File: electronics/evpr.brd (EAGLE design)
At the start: 97.2 x 71.7 mm, 89 parts, among them J1 10118193-0001LF, J2 B4P-VH(LF)(SN), Q1 AOD4184A, Q2 AOD4184A, T1 MMBT2222A, T2 MMBT2222A, T3 MMBT2222A, T5 MMBT2222A, U1 MC14044BDR2G, U2 BQ2057TTS, U3 ESP32-WROOM-32D, U5 AP2112K-3.3TRG1, U6 SN74AHCT125DR, U7 TPSM84824MOLR, U8 LTC4353CMSPBFMSOP-16_MS-M, X1 B3P-VH(LF)(SN), X2 B3P-VH(LF)(SN), X3 B3P-VH(LF)(SN)

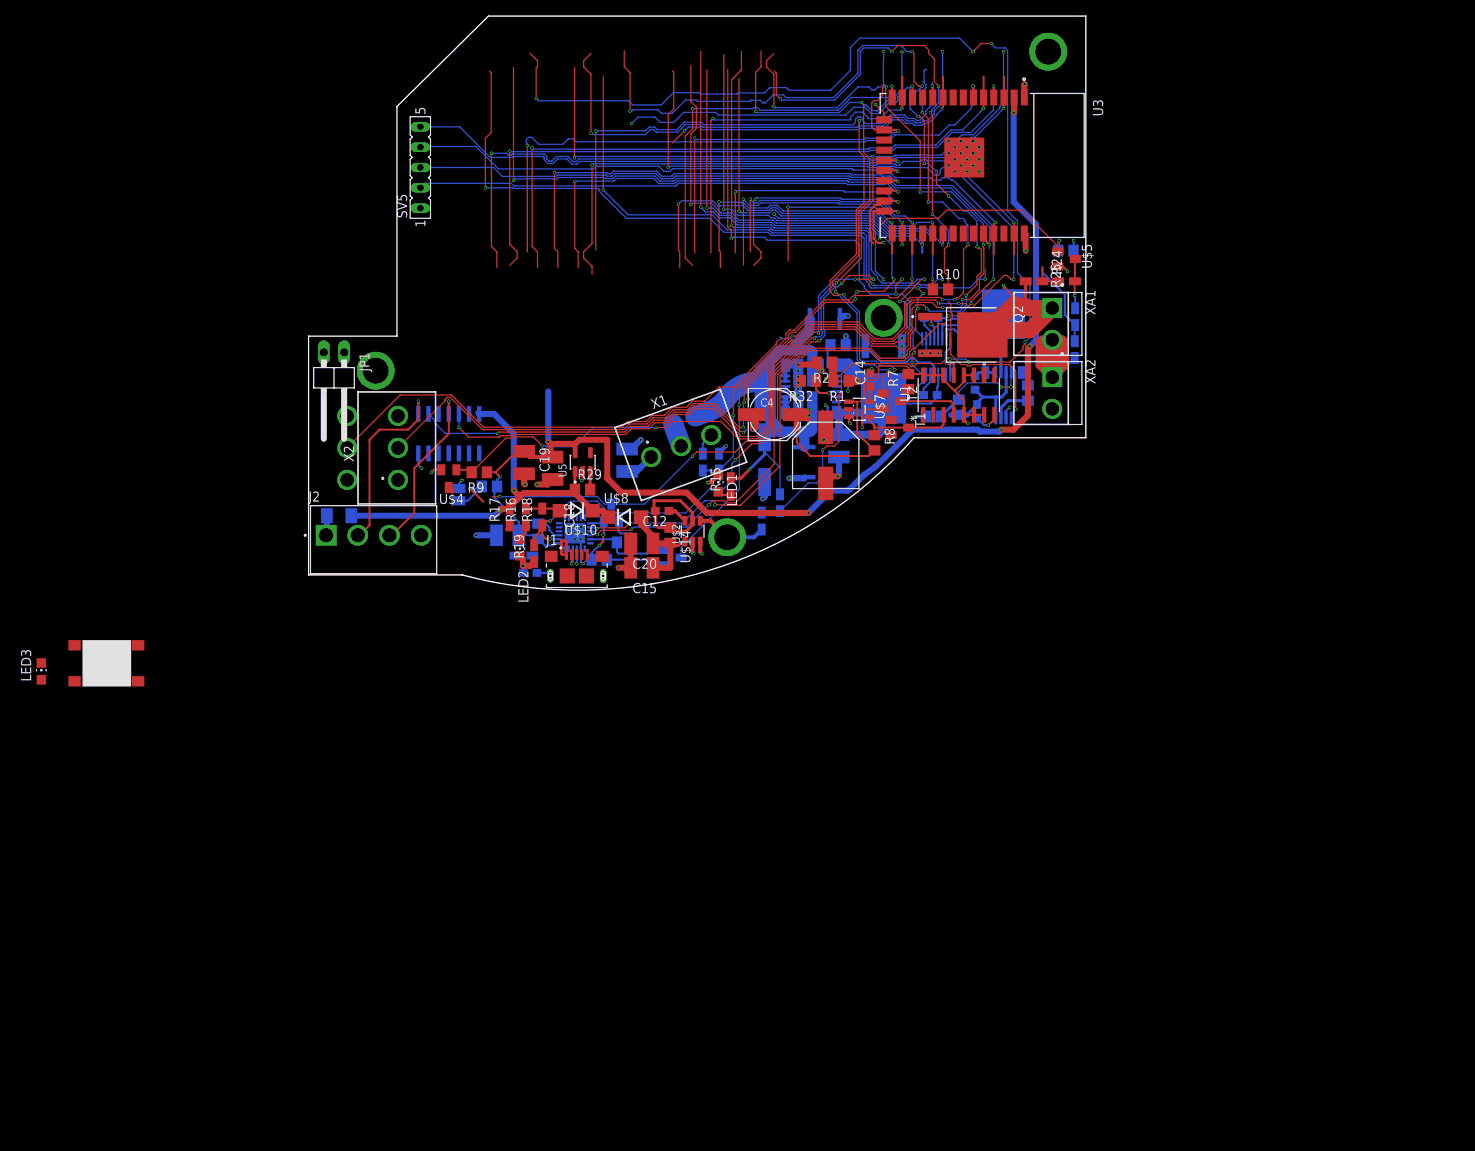
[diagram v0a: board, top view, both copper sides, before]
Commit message: Fixed power save for battery sensing
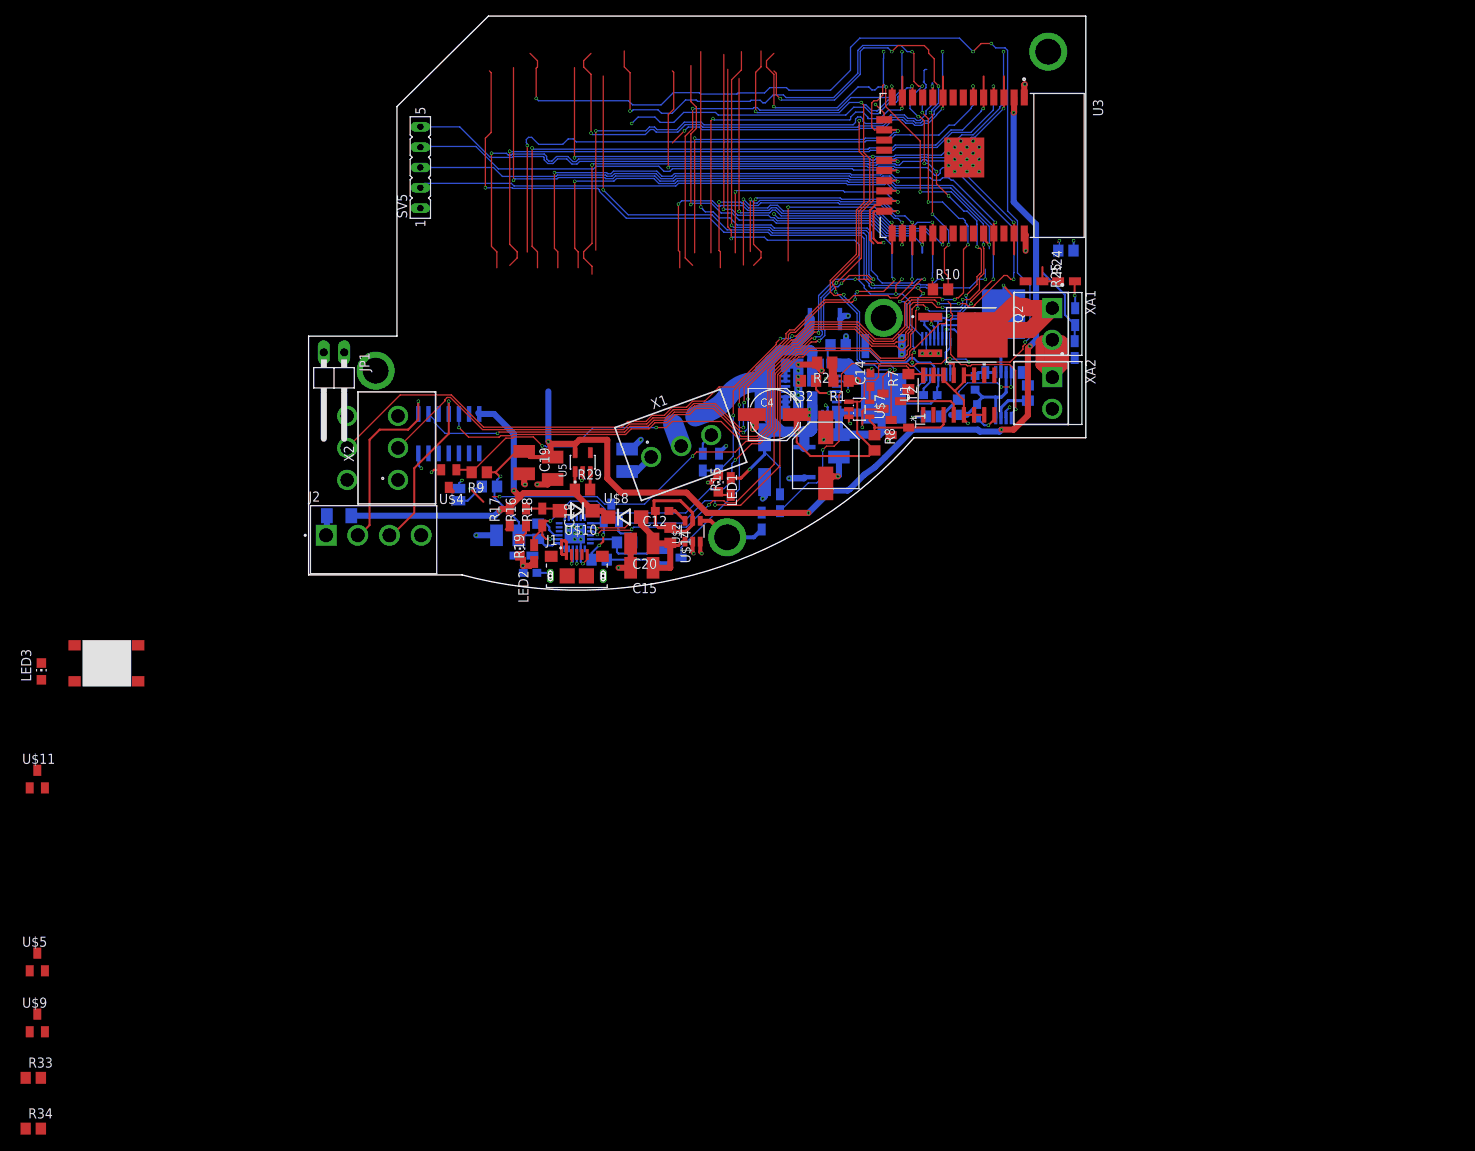
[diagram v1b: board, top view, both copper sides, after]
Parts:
- added R33, R34: 100k, rcl:R0805
- added U$11: DMN5L06K-7, mccloud:SOT23
- added U$9: BSS84-7-F, mccloud:SOT23
- U$5: value DMN5L06K-7 -> BSS84-7-F
- moved U$5 155.8 mm to (-67.6, -102.4), turned to 0 degrees
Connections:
- new net N$13: R24.2, U$9.3
- new net N$35: R33.2, U$11.3, U$5.1, U$9.1
- net GND: now also R25.1, R27.1, R34.2, U$11.2; no longer U$5.2
- net N$33: now also R26.2; no longer R25.1, R27.1
- net N$8: now also U$5.2; no longer R26.2
- net POWERSAVE: now also R34.1, U$11.1; no longer U$5.1
- net VBAT: now also R33.1, U$9.2; no longer R24.2
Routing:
- net POWERSAVE: track 112.5 -> 37.3 mm, vias 7 -> 4
- net N$33: track 6.22 -> 0.00 mm, vias 1 -> 0
- net N$8: track 21.8 -> 18.4 mm
- net VBAT: track 56.1 -> 53.5 mm
- net GND: track 109.5 -> 111.4 mm

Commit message: routing and board fixes
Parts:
- added U$13, U$15: LSM115J, mccloud:DO214BA
- C1: value 10sµF -> 10µF
- moved R34 98.1 mm to (1.27, -53.8), turned to 180 degrees
- moved XA1 92.9 mm to (-29.5, -50.0), turned to 180 degrees
- moved XA2 89.8 mm to (-29.5, -44.7), flipped to the bottom, turned to 180 degrees
- moved R33 85.8 mm to (-14.0, -50.3), flipped to the bottom, turned to 180 degrees
- moved U$9 80.3 mm to (-11.4, -52.6), flipped to the bottom, turned to 270 degrees
- moved U$5 77.8 mm to (-10.4, -49.5), flipped to the bottom, turned to 90 degrees
- moved U$3 77.7 mm to (-19.8, -50.3), flipped to the top, turned to 90 degrees
- moved X3 76.4 mm to (45.2, -57.0), turned to 0 degrees
- moved U$11 74.2 mm to (1.14, -51.4), turned to 90 degrees
- moved Q2 73.0 mm to (-19.8, -50.5), flipped to the bottom
- moved R26 72.5 mm to (-6.35, -49.5), turned to 0 degrees
- moved R4 71.8 mm to (-12.2, -52.8), flipped to the top, turned to 180 degrees
- moved R14 70.9 mm to (55.8, -5.08)
- moved T3 70.8 mm to (57.5, 0.25)
- moved U$12 69.6 mm to (51.1, -1.91), turned to 180 degrees
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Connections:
- new net AGND: R2.2, R31.2, R32.2, U7.23, U7.3, U7.9
- new net N$43: R7.2, R8.2, U$13.C, U$15.C, U1.11, U1.12, U1.14, U1.15, U1.16, U1.5, U1.6, U1.7
- net GND: no longer R2.2, R31.2, R32.2, U7.23, U7.3, U7.9
- net VBAT: now also U$15.A
- net VRAW: now also U$13.A; no longer R7.2, R8.2, U1.11, U1.12, U1.14, U1.15, U1.16, U1.5, U1.6, U1.7
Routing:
- net RESET: track 248.2 -> 0.00 mm, vias 10 -> 0
- net SERVO1: track 240.6 -> 0.00 mm, vias 8 -> 0
- net RAWSENSE: track 236.7 -> 0.00 mm, vias 9 -> 0
- net ESP_TX: track 231.3 -> 0.00 mm, vias 9 -> 0
- net ESP_RX: track 224.1 -> 0.00 mm, vias 10 -> 0
- net DS_DAT: track 212.7 -> 0.00 mm, vias 13 -> 0
- net DS_CLK: track 198.5 -> 0.00 mm, vias 12 -> 0
- net SERVO2: track 189.6 -> 0.00 mm, vias 9 -> 0
- net RST_DISABLE: track 182.6 -> 0.00 mm, vias 9 -> 0
- net USBSENSE: track 152.7 -> 0.00 mm, vias 9 -> 0
- net SHUTDOWN_CANCEL: track 150.9 -> 0.00 mm, vias 7 -> 0
- net 3.3V: track 149.9 -> 0.00 mm, vias 6 -> 0
- net CSTAT: track 130.8 -> 0.00 mm, vias 9 -> 0
- net BOOTMODE: track 124.0 -> 0.00 mm, vias 7 -> 0
- net SHUTDOWN: track 123.1 -> 0.00 mm, vias 7 -> 0
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
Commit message: Whew. Lots of routing. Lots of minor circuit changes. Routing is 99% done, just finishing touches are remaining.
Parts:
- removed R11: 10k, rcl:R0805
- added C11, C21: 0.1uF, eagle-ltspice:C0603
- U$13: value LSM115J -> SDM40E20LC; device mccloud:DO214BA -> mccloud:SOT23
- U$15: value LSM115J -> 1000µF; device mccloud:DO214BA -> mccloud:810RADCAN
- moved C13 111.7 mm to (-8.89, -48.4), flipped to the top, turned to 0 degrees
- moved R25 111.7 mm to (-2.41, -52.6), flipped to the bottom, turned to 0 degrees
- moved R24 107.8 mm to (-6.35, -54.4), flipped to the bottom, turned to 0 degrees
- moved R15 106.9 mm to (-27.4, -41.6), turned to 0 degrees
- moved LED3 105.9 mm to (34.5, -36.3), flipped to the bottom
- moved R1 102.1 mm to (-12.7, -37.3), turned to 90 degrees
- moved U$1 102.0 mm to (35.1, -25.4)
- moved R32 101.6 mm to (-16.3, -37.3), turned to 90 degrees
- moved R2 100.9 mm to (-14.5, -37.3), turned to 270 degrees
- moved C5 96.8 mm to (-2.92, -37.7), turned to 180 degrees
- moved C10 96.8 mm to (-4.83, -39.4), turned to 180 degrees
- moved C9 94.8 mm to (43.9, -19.3), flipped to the top
- moved J1 92.6 mm to (38.4, -19.3), flipped to the bottom, turned to 180 degrees
- moved LED1 91.5 mm to (-31.1, -41.6), turned to 90 degrees
- moved J2 90.1 mm to (49.7, -32.3)
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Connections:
- net 5.0V: now also C21.2
- net GND: now also C11.1, C21.1, U$15.C$2; no longer R11.1
- net N$28: now also U$15.A$1
- net N$43: now also C11.2, U$13.3; no longer U$13.C, U$15.C
- net POWERSAVE: no longer R11.2
- net VBAT: now also U$13.1; no longer U$15.A
- net VRAW: now also U$13.2; no longer U$13.A
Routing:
- net CSTAT: track 0.00 -> 51.0 mm, vias 0 -> 2
- net 3.3V: track 0.00 -> 49.2 mm, vias 0 -> 4
- net VRAW: track 71.8 -> 120.9 mm, vias 8 -> 14
- net POWERSAVE: track 0.00 -> 49.0 mm, vias 0 -> 1
- net USING_BAT: track 0.00 -> 48.7 mm, vias 0 -> 2
- net 5.0V: track 0.00 -> 46.6 mm, vias 0 -> 3
- net VCONV: track 40.2 -> 85.0 mm, vias 8 -> 10
- net USING_ENG: track 0.00 -> 42.2 mm, vias 0 -> 2
- net TACH: track 38.6 -> 78.2 mm, vias 0 -> 2
- net RESET: track 0.00 -> 39.5 mm, vias 0 -> 3
- net N$43: track 0.00 -> 34.9 mm, vias 0 -> 1
- net VBAT: track 28.1 -> 59.6 mm, vias 0 -> 5
- net RAWSENSE: track 0.00 -> 26.5 mm, vias 0 -> 2
- net BATSENSE1: track 0.00 -> 26.4 mm, vias 0 -> 2
- net BATSENSE2: track 0.00 -> 23.5 mm, vias 0 -> 2
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- added copper zone on layer 1, net AGND
- added copper zone on layer 15, net AGND
- added copper zone on layer 16, net AGND
- added copper zone on layer 1, net AVOID1

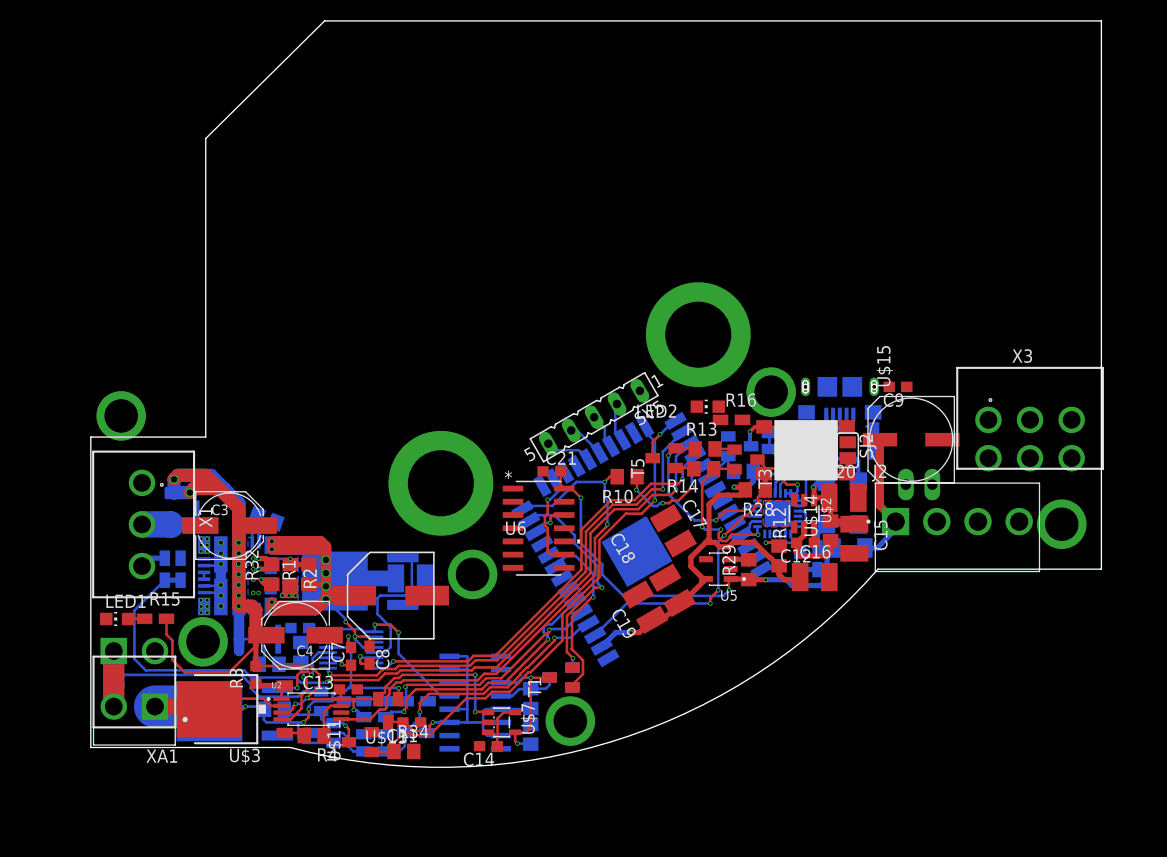
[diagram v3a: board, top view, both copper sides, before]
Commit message: Routing complete. All DRC/ERC checks except for USB port silliness performed and resolved. Test points added.
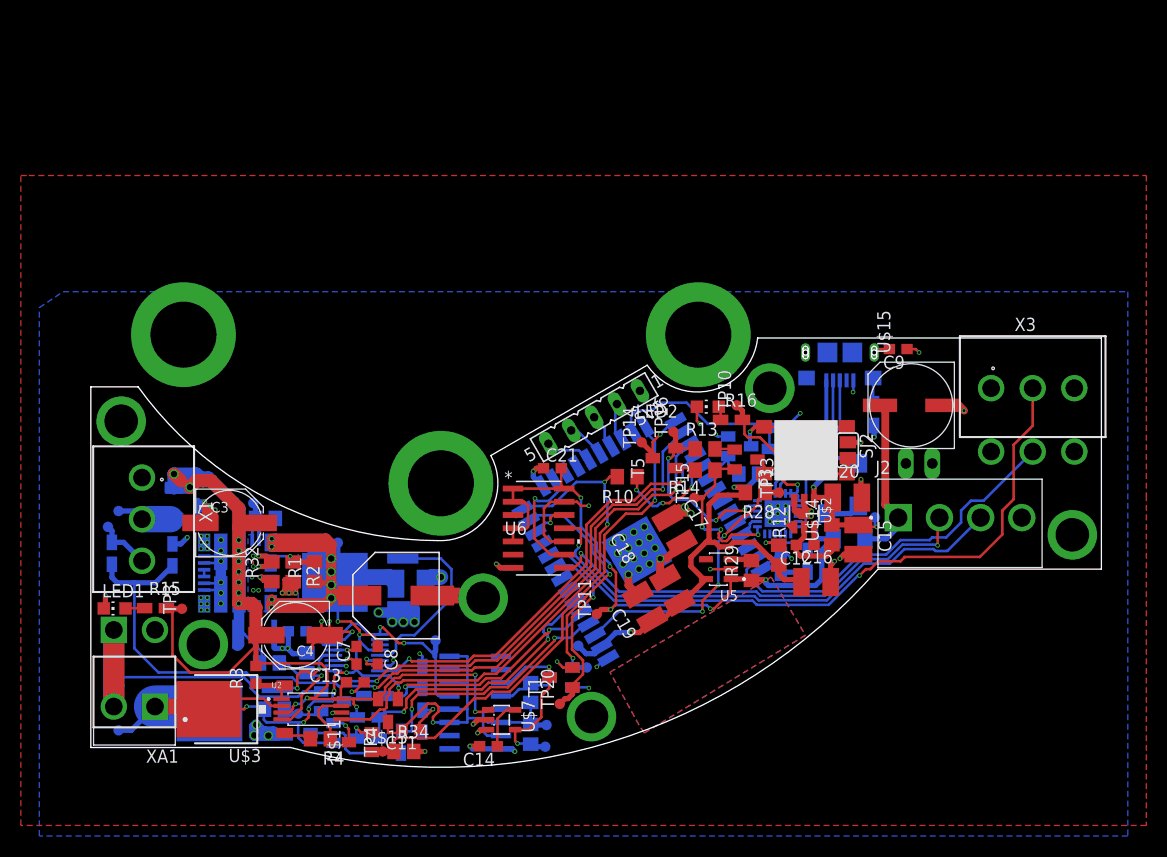
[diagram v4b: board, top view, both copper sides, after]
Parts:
- added TP1, TP10, TP11, TP12, TP13, TP14, TP15, TP16, TP19, TP2, TP20, TP21, TP22, TP23, TP3, TP4, TP5, TP6, TP7, TP8, TP9: PTR1TP10R, testpad:TP10R
- moved R22 5.30 mm to (-31.6, -35.3)
- moved C9 3.63 mm to (44.0, -15.7)
- moved J1 3.30 mm to (38.4, -16.0)
- moved U$15 3.30 mm to (45.2, -21.1)
- moved X3 3.06 mm to (56.9, -19.4)
- moved R24 2.67 mm to (-3.84, -53.5), turned to 270 degrees
- moved R30 2.54 mm to (41.7, -22.0)
- moved R27 2.34 mm to (-1.78, -47.2), turned to 270 degrees
- moved XA2 2.03 mm to (-29.5, -42.7)
- moved JP1 2.03 mm to (46.0, -22.9)
- moved LED3 1.85 mm to (32.7, -36.3)
- moved U$10 1.78 mm to (40.1, -28.7)
- moved R23 1.58 mm to (-25.8, -35.5)
- moved R25 1.31 mm to (-1.78, -51.4), turned to 270 degrees
- moved R6 1.15 mm to (-12.9, -45.8)
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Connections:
- net 3.3V: now also TP12.TP
- net 5.0V: now also TP11.TP, U6.1, U6.2, U6.4, U6.5
- net AGND: now also TP7.TP
- net BOOTMODE: now also TP14.TP
- net GND: now also U6.10, U6.13
- net N$11: now also TP22.TP
- net N$14: now also TP10.TP
- net N$18: now also TP15.TP
- net N$19: now also TP16.TP
- net N$30: now also TP21.TP
- net N$35: now also TP8.TP
- net N$43: now also TP23.TP
- net N$51: now also TP9.TP
- net POWERSAVE: now also TP4.TP
- net RESET: now also TP13.TP
- net SHUTDOWN: now also TP19.TP
- net SHUTDOWN_CANCEL: now also TP20.TP
- net TACH_RAW: now also TP2.TP
- net USBD+: no longer J1.4
- net VBAT: now also TP6.TP
- net VCONV: now also TP5.TP
- net VRAW: now also TP3.TP
- net VRAW_PF: now also TP1.TP
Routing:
- net GND: track 10.6 -> 119.7 mm, vias 24 -> 89
- net SERVO2: track 0.00 -> 63.8 mm, vias 0 -> 1
- net N$22: track 0.00 -> 48.6 mm, vias 0 -> 1
- net N$27: track 0.00 -> 43.4 mm, vias 0 -> 2
- net SERVO1: track 0.00 -> 36.4 mm
- net SYS_POWER: track 0.00 -> 36.3 mm, vias 0 -> 13
- net 5.0V: track 46.6 -> 68.7 mm, vias 3 -> 5
- net VCONV: track 85.0 -> 106.7 mm
- net USBSENSE: track 10.2 -> 27.3 mm
- net N$14: track 12.0 -> 24.8 mm, vias 2 -> 3
- net N$43: track 34.9 -> 41.0 mm
- net VRAW_PF: track 2.79 -> 8.16 mm
- net VRAW: track 120.9 -> 126.1 mm
- net N$11: track 13.8 -> 18.7 mm
- net TACH: track 78.2 -> 83.0 mm
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- added copper zone on layer 1, net GND
- added copper zone on layer 16, net GND
- removed copper zone on layer 1, net AVOID1
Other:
- board size 97.2 x 71.7 mm -> 97.2 x 41.3 mm
